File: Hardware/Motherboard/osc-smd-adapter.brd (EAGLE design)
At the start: 20.3 x 12.7 mm, 2 parts

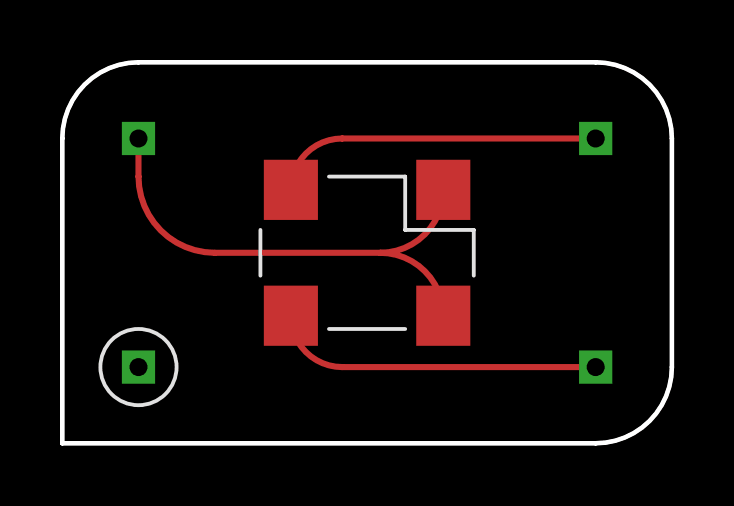
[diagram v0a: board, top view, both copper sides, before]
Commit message: Fix flipped SMD oscillator
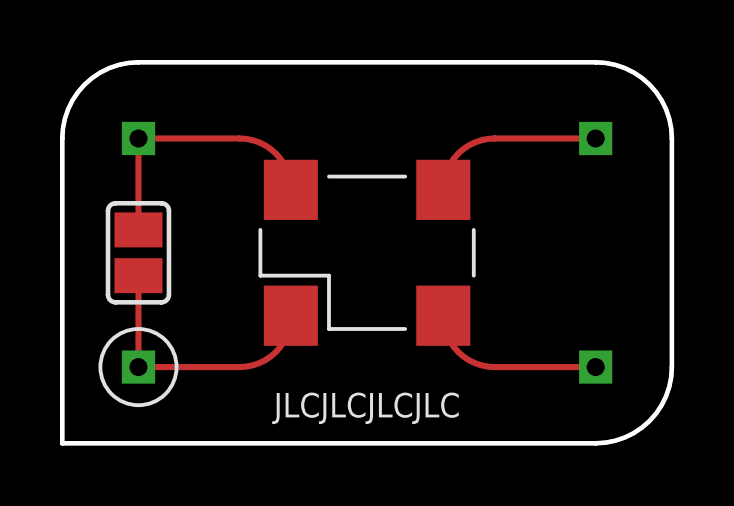
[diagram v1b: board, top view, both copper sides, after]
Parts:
- added SJ1: (no value), jumper:SJ
- turned U$1 to 0 degrees
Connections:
- new net N$4: SJ1.2, U$1.P$1, U$2.P$1
- net N$1: now also SJ1.1; no longer U$1.P$1
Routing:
- net N$4: track 0.00 -> 8.84 mm
- net N$1: track 16.3 -> 8.84 mm
- net N$3: track 10.9 -> 5.79 mm
- net N$2: track 10.9 -> 5.79 mm
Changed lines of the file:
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@@
 <wire x1="2.54" y1="12.7" x2="0" y2="10.16" width="0.1524" layer="20" curve="90"/>
 <wire x1="0" y1="10.16" x2="0" y2="0" width="0.1524" layer="20"/>
-<text x="10.16" y="1.27" size="0.8128" layer="26" font="vector" rot="MR0" align="center">JLCJLCJLCJLC</text>
+<text x="10.16" y="1.27" size="0.8128" layer="25" font="vector" align="center">JLCJLCJLCJLC</text>
 <text x="10.16" y="6.35" size="1.27" layer="26" font="vector" rot="MR0" align="center">SMD-THT
 Oscillator Adapter</text>
@@
 </autorouter>
 <elements>
-<element name="U$1" library="0_gametankparts" package="OSCPADS" value="OSC2" x="10.16" y="6.35" smashed="yes" rot="R180"/>
+<element name="U$1" library="0_gametankparts" package="OSCPADS" value="OSC2" x="10.16" y="6.35" smashed="yes"/>
 <element name="U$2" library="0_gametankparts" package="CRYSTAL800MIL" value="OSCILLATORMODULEDIL14" x="2.54" y="2.54" smashed="yes"/>
+<element name="SJ1" library="jumper" library_urn="urn:adsk.eagle:library:252" package="SJ" package3d_urn="urn:adsk.eagle:package:15471/1" value="" x="2.54" y="6.35" smashed="yes" rot="R270">
+<attribute name="POPULARITY" value="33" x="2.54" y="6.35" size="0.8128" layer="27" rot="R270" display="off"/>
+<attribute name="VALUE" x="2.54" y="5.9499" size="0.02" layer="27" rot="R270"/>
+</element>
 </elements>
 <signals>
+<signal name="N$2">
+<contactref element="U$1" pad="P$3"/>
+<contactref element="U$2" pad="P$4"/>
+<wire x1="12.7" y1="8.448040625" x2="14.411959375" y2="10.16" width="0.2032" layer="1" curve="-90"/>
+<wire x1="14.411959375" y1="10.16" x2="17.78" y2="10.16" width="0.2032" layer="1"/>
+</signal>
+<signal name="N$3">
+<contactref element="U$1" pad="P$2"/>
+<contactref element="U$2" pad="P$2"/>
+<wire x1="12.7" y1="4.251959375" x2="14.411959375" y2="2.54" width="0.2032" layer="1" curve="90"/>
+<wire x1="14.411959375" y1="2.54" x2="17.78" y2="2.54" width="0.2032" layer="1"/>
+</signal>
 <signal name="N$1">
 <contactref element="U$1" pad="P$4"/>
 <contactref element="U$2" pad="P$3"/>
+<wire x1="7.62" y1="8.448040625" x2="5.908040625" y2="10.16" width="0.2032" layer="1" curve="90"/>
+<wire x1="5.908040625" y1="10.16" x2="2.54" y2="10.16" width="0.2032" layer="1"/>
+<contactref element="SJ1" pad="1"/>
+<wire x1="2.54" y1="10.16" x2="2.54" y2="7.112" width="0.2032" layer="1"/>
+</signal>
+<signal name="N$4">
 <contactref element="U$1" pad="P$1"/>
-<wire x1="2.54" y1="10.16" x2="2.54" y2="8.89" width="0.2032" layer="1"/>
-<wire x1="2.54" y1="8.89" x2="5.08" y2="6.35" width="0.2032" layer="1" curve="90"/>
-<wire x1="10.601959375" y1="6.35" x2="12.7" y2="8.448040625" width="0.2032" layer="1" curve="90"/>
-<wire x1="5.08" y1="6.35" x2="10.601959375" y2="6.35" width="0.2032" layer="1"/>
-<wire x1="10.601959375" y1="6.35" x2="12.7" y2="4.251959375" width="0.2032" layer="1" curve="-90"/>
-</signal>
-<signal name="N$2">
-<contactref element="U$1" pad="P$3"/>
-<contactref element="U$2" pad="P$4"/>
-<wire x1="7.62" y1="8.448040625" x2="9.331959375" y2="10.16" width="0.2032" layer="1" curve="-90"/>
-<wire x1="9.331959375" y1="10.16" x2="17.78" y2="10.16" width="0.2032" layer="1"/>
-</signal>
-<signal name="N$3">
-<contactref element="U$1" pad="P$2"/>
-<contactref element="U$2" pad="P$2"/>
-<wire x1="7.62" y1="4.251959375" x2="9.331959375" y2="2.54" width="0.2032" layer="1" curve="90"/>
-<wire x1="9.331959375" y1="2.54" x2="17.78" y2="2.54" width="0.2032" layer="1"/>
+<contactref element="U$2" pad="P$1"/>
+<wire x1="7.62" y1="4.251959375" x2="5.908040625" y2="2.54" width="0.2032" layer="1" curve="-90"/>
+<wire x1="5.908040625" y1="2.54" x2="2.54" y2="2.54" width="0.2032" layer="1"/>
+<contactref element="SJ1" pad="2"/>
+<wire x1="2.54" y1="5.588" x2="2.54" y2="2.54" width="0.2032" layer="1"/>
 </signal>
 </signals>
@@
 which will not be processed correctly with this version.
 </note>
+<note version="8.2" severity="warning">
+Since Version 8.2, EAGLE supports online libraries. The ids
+of those online libraries will not be understood (or retained)
+with this version.
+</note>
+<note version="8.3" severity="warning">
+Since Version 8.3, EAGLE supports URNs for individual library
+assets (packages, symbols, and devices). The URNs of those assets
+will not be understood (or retained) with this version.
+</note>
+<note version="8.3" severity="warning">
+Since Version 8.3, EAGLE supports the association of 3D packages
+with devices in libraries, schematics, and board files. Those 3D
+packages will not be understood (or retained) with this version.
+</note>
 </compatibility>
